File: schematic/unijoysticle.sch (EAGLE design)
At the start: 8 parts, among them IC1 4066N, IC2 4066N, IC3 4066N, J1 DB9, J2 DB9, J3 POWER_JACKSLT

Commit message: PCB fixes: reduced realstate
uses new DB9 connectors without the uneeded holes.
compabible with Commodore 128D and SX-64
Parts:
- J1, J2: device SparkFun-Connectors:DB9FEMALE -> riq-connectors:DB9FEMALE
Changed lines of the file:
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@@
 <part name="GND1" library="SparkFun-Aesthetics" deviceset="GND2" device=""/>
 <part name="GND2" library="SparkFun-Aesthetics" deviceset="GND2" device=""/>
-<part name="J1" library="SparkFun-Connectors" deviceset="DB9" device="FEMALE" value="DB9">
+<part name="J1" library="riq-connectors" deviceset="DB9" device="FEMALE" value="DB9">
 <attribute name="MF" value=""/>
 <attribute name="MPN" value="618009231121"/>
 <attribute name="OC_NEWARK" value="16T0655"/>
 </part>
-<part name="J2" library="SparkFun-Connectors" deviceset="DB9" device="FEMALE" value="DB9">
+<part name="J2" library="riq-connectors" deviceset="DB9" device="FEMALE" value="DB9">
 <attribute name="MF" value=""/>
 <attribute name="MPN" value="618009231121"/>

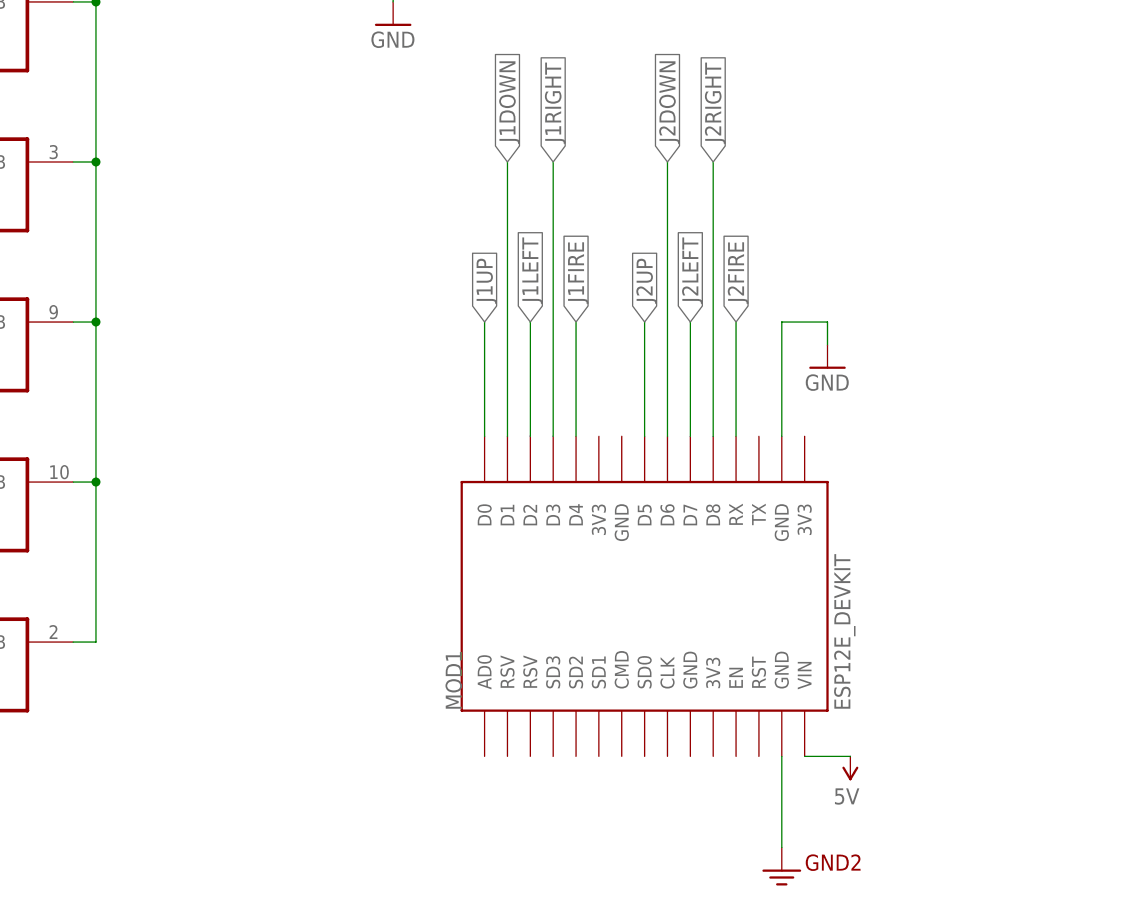
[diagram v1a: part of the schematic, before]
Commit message: using wemos d1 mini instead of NodeMCU
smaller realstate PCB making it under 5cm by 5cm.
cheaper to order from certain providers
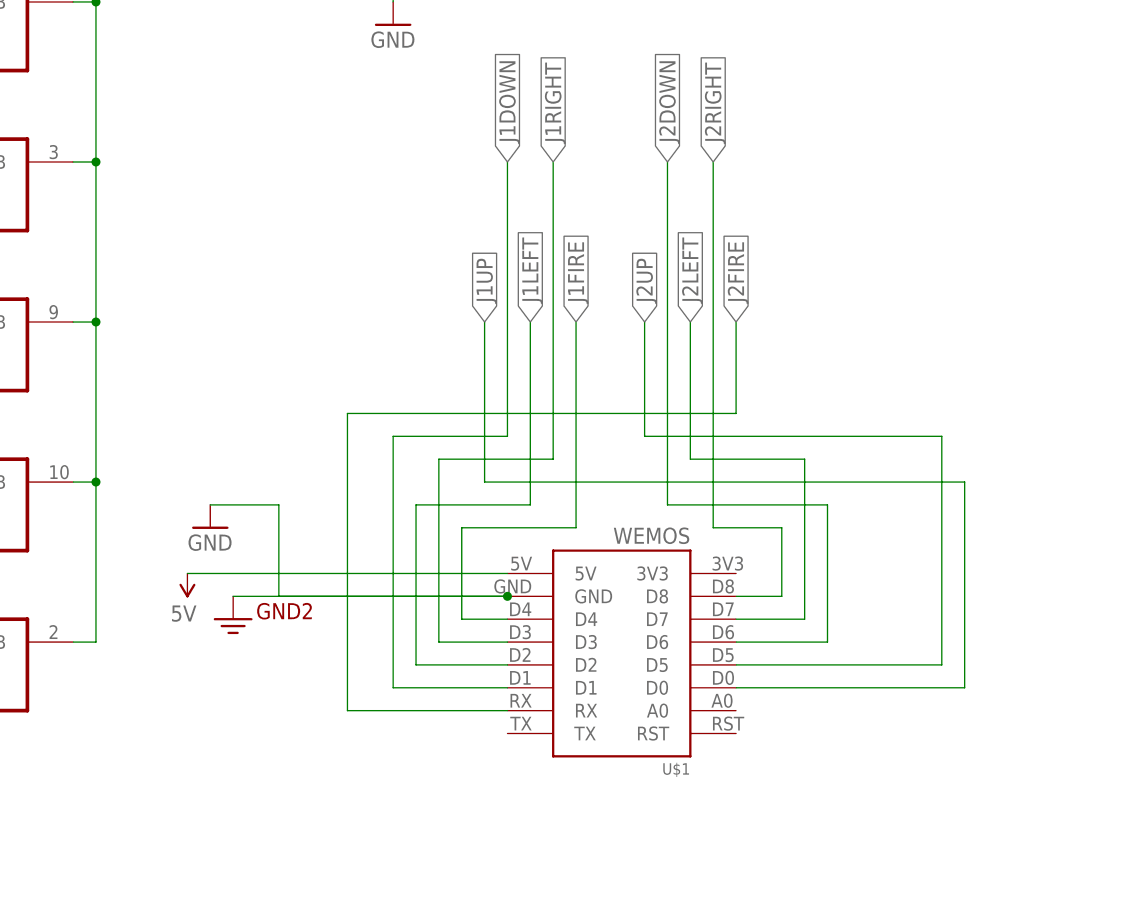
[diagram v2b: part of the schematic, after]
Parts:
- removed MOD1: ESP12E_DEVKIT, ESP12E_DEVKIT:ESP12E_DEVKIT
- added U$1: WEMOS, 1455413453956-wemos:WEMOS
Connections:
- net 3.3V: no longer MOD1.GND@1
- net 5V: now also U$1.5V; no longer MOD1.VIN
- net GND: now also U$1.GND; no longer MOD1.GND@3
- net J1DOWN: now also U$1.D1; no longer MOD1.D1
- net J1FIRE: now also U$1.D4; no longer MOD1.D4
- net J1LEFT: now also U$1.D2; no longer MOD1.D2
- net J1RIGHT: now also U$1.D3; no longer MOD1.D3
- net J1UP: now also U$1.D0; no longer MOD1.D0
- net J2DOWN: now also U$1.D6; no longer MOD1.D6
- net J2FIRE: now also U$1.RX; no longer MOD1.RX
- net J2LEFT: now also U$1.D7; no longer MOD1.D7
- net J2RIGHT: now also U$1.D8; no longer MOD1.D8
- net J2UP: now also U$1.D5; no longer MOD1.D5
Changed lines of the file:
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@@
 <attributes>
 <attribute name="CNAME" value="Retro Moe"/>
-<attribute name="CREVISION" value="0.2.2"/>
+<attribute name="CREVISION" value="0.3.2"/>
 <attribute name="DESIGNER" value="Ricardo Quesada"/>
 </attributes>
@@
 <attribute name="OC_NEWARK" value="16T0655"/>
 </part>
-<part name="MOD1" library="ESP12E_DEVKIT" deviceset="ESP12E_DEVKIT" device=""/>
 <part name="FRAME1" library="SparkFun-Aesthetics" deviceset="FRAME-A4L" device=""/>
 <part name="J3" library="SparkFun-Connectors" deviceset="POWER_JACK" device="SLT"/>
@@
 <part name="GND5" library="SparkFun-Aesthetics" deviceset="GND" device=""/>
 <part name="GND6" library="SparkFun-Aesthetics" deviceset="GND" device=""/>
+<part name="U$1" library="1455413453956-wemos" deviceset="WEMOS" device=""/>
 </parts>
 <sheets>
@@
 <instance part="IC1" gate="P" x="101.6" y="142.24"/>
 <instance part="IC3" gate="P" x="109.22" y="139.7"/>
-<instance part="GND3" gate="1" x="149.86" y="86.36"/>
+<instance part="GND3" gate="1" x="81.28" y="68.58"/>
 <instance part="GND4" gate="1" x="101.6" y="124.46"/>
 <instance part="IC2" gate="A" x="53.34" y="53.34">
@@
 </instance>
 <instance part="SUPPLY1" gate="G$1" x="175.26" y="144.78"/>
-<instance part="SUPPLY2" gate="G$1" x="152.4" y="43.18" rot="R180"/>
+<instance part="SUPPLY2" gate="G$1" x="78.74" y="63.5" rot="R180"/>
 <instance part="GND1" gate="G$1" x="177.8" y="137.16"/>
-<instance part="GND2" gate="G$1" x="144.78" y="30.48"/>
+<instance part="GND2" gate="G$1" x="83.82" y="58.42"/>
 <instance part="J1" gate="G$1" x="53.34" y="157.48">
 <attribute name="OC_NEWARK" x="53.34" y="157.48" size="1.778" layer="96" display="off"/>
@@
 <attribute name="MPN" x="233.68" y="152.4" size="1.778" layer="96" display="off"/>
 </instance>
-<instance part="MOD1" gate="G$1" x="129.54" y="60.96" rot="R90"/>
 <instance part="FRAME1" gate="G$1" x="0" y="0"/>
 <instance part="J3" gate="G$1" x="144.78" y="137.16"/>
@@
 <instance part="GND5" gate="1" x="256.54" y="147.32"/>
 <instance part="GND6" gate="1" x="76.2" y="152.4"/>
+<instance part="U$1" gate="G$1" x="134.62" y="66.04" rot="R180"/>
 </instances>
 <busses>
@@
 </segment>
 <segment>
-<pinref part="MOD1" gate="G$1" pin="D0"/>
-<wire x1="111.76" y1="78.74" x2="111.76" y2="91.44" width="0.1524" layer="91"/>
+<wire x1="111.76" y1="73.66" x2="111.76" y2="91.44" width="0.1524" layer="91"/>
 <label x="111.76" y="91.44" size="1.778" layer="95" rot="R90" xref="yes"/>
+<wire x1="111.76" y1="73.66" x2="165.1" y2="73.66" width="0.1524" layer="91"/>
+<wire x1="165.1" y1="73.66" x2="165.1" y2="50.8" width="0.1524" layer="91"/>
+<pinref part="U$1" gate="G$1" pin="D0"/>
+<wire x1="165.1" y1="50.8" x2="139.7" y2="50.8" width="0.1524" layer="91"/>
 </segment>
 </net>
@@
 </segment>
 <segment>
-<pinref part="MOD1" gate="G$1" pin="D1"/>
 <label x="114.3" y="109.22" size="1.778" layer="95" rot="R90" xref="yes"/>
 <wire x1="114.3" y1="78.74" x2="114.3" y2="109.22" width="0.1524" layer="91"/>
+<wire x1="114.3" y1="78.74" x2="101.6" y2="78.74" width="0.1524" layer="91"/>
+<wire x1="101.6" y1="78.74" x2="101.6" y2="50.8" width="0.1524" layer="91"/>
+<pinref part="U$1" gate="G$1" pin="D1"/>
+<wire x1="101.6" y1="50.8" x2="114.3" y2="50.8" width="0.1524" layer="91"/>
 </segment>
 </net>
@@
 </segment>
 <segment>
-<wire x1="116.84" y1="78.74" x2="116.84" y2="91.44" width="0.1524" layer="91"/>
-<pinref part="MOD1" gate="G$1" pin="D2"/>
+<wire x1="116.84" y1="71.12" x2="116.84" y2="91.44" width="0.1524" layer="91"/>
 <label x="116.84" y="91.44" size="1.778" layer="95" rot="R90" xref="yes"/>
+<wire x1="116.84" y1="71.12" x2="104.14" y2="71.12" width="0.1524" layer="91"/>
+<wire x1="104.14" y1="71.12" x2="104.14" y2="53.34" width="0.1524" layer="91"/>
+<pinref part="U$1" gate="G$1" pin="D2"/>
+<wire x1="104.14" y1="53.34" x2="114.3" y2="53.34" width="0.1524" layer="91"/>
 </segment>
 </net>
@@
 </segment>
 <segment>
-<pinref part="MOD1" gate="G$1" pin="D3"/>
 <label x="119.38" y="109.22" size="1.778" layer="95" rot="R90" xref="yes"/>
-<wire x1="119.38" y1="109.22" x2="119.38" y2="78.74" width="0.1524" layer="91"/>
+<wire x1="119.38" y1="109.22" x2="119.38" y2="76.2" width="0.1524" layer="91"/>
+<wire x1="119.38" y1="76.2" x2="106.68" y2="76.2" width="0.1524" layer="91"/>
+<wire x1="106.68" y1="76.2" x2="106.68" y2="55.88" width="0.1524" layer="91"/>
+<pinref part="U$1" gate="G$1" pin="D3"/>
+<wire x1="106.68" y1="55.88" x2="114.3" y2="55.88" width="0.1524" layer="91"/>
 </segment>
 </net>
@@
 </segment>
 <segment>
-<wire x1="144.78" y1="78.74" x2="144.78" y2="91.44" width="0.1524" layer="91"/>
-<wire x1="144.78" y1="91.44" x2="149.86" y2="91.44" width="0.1524" layer="91"/>
 <pinref part="GND3" gate="1" pin="GND"/>
-<wire x1="149.86" y1="91.44" x2="149.86" y2="88.9" width="0.1524" layer="91"/>
-<pinref part="MOD1" gate="G$1" pin="GND@3"/>
+<pinref part="GND2" gate="G$1" pin="3.3V"/>
+<wire x1="83.82" y1="60.96" x2="114.3" y2="60.96" width="0.1524" layer="91"/>
+<pinref part="U$1" gate="G$1" pin="GND"/>
+<wire x1="81.28" y1="71.12" x2="88.9" y2="71.12" width="0.1524" layer="91"/>
+<wire x1="88.9" y1="71.12" x2="88.9" y2="60.96" width="0.1524" layer="91"/>
+<wire x1="88.9" y1="60.96" x2="114.3" y2="60.96" width="0.1524" layer="91"/>
+<junction x="114.3" y="60.96"/>
 </segment>
 <segment>
@@
 <segment>
 <pinref part="SUPPLY2" gate="G$1" pin="5V"/>
-<wire x1="152.4" y1="43.18" x2="147.32" y2="43.18" width="0.1524" layer="91"/>
-<pinref part="MOD1" gate="G$1" pin="VIN"/>
+<wire x1="78.74" y1="63.5" x2="114.3" y2="63.5" width="0.1524" layer="91"/>
+<pinref part="U$1" gate="G$1" pin="5V"/>
 </segment>
 </net>
@@
 <junction x="147.32" y="139.7"/>
 </segment>
-<segment>
-<pinref part="GND2" gate="G$1" pin="3.3V"/>
-<wire x1="144.78" y1="33.02" x2="144.78" y2="43.18" width="0.1524" layer="91"/>
-<pinref part="MOD1" gate="G$1" pin="GND@1"/>
-</segment>
 </net>
 <net name="J1FIRE" class="0">
@@
 </segment>
 <segment>
-<wire x1="121.92" y1="91.44" x2="121.92" y2="78.74" width="0.1524" layer="91"/>
-<pinref part="MOD1" gate="G$1" pin="D4"/>
+<wire x1="121.92" y1="91.44" x2="121.92" y2="68.58" width="0.1524" layer="91"/>
 <label x="121.92" y="91.44" size="1.778" layer="95" rot="R90" xref="yes"/>
+<wire x1="121.92" y1="68.58" x2="109.22" y2="68.58" width="0.1524" layer="91"/>
+<wire x1="109.22" y1="68.58" x2="109.22" y2="58.42" width="0.1524" layer="91"/>
+<pinref part="U$1" gate="G$1" pin="D4"/>
+<wire x1="109.22" y1="58.42" x2="114.3" y2="58.42" width="0.1524" layer="91"/>
 </segment>
 </net>
 <net name="J2UP" class="0">
 <segment>
-<pinref part="MOD1" gate="G$1" pin="D5"/>
 <wire x1="129.54" y1="78.74" x2="129.54" y2="91.44" width="0.1524" layer="91"/>
 <label x="129.54" y="91.44" size="1.778" layer="95" rot="R90" xref="yes"/>
+<pinref part="U$1" gate="G$1" pin="D5"/>
+<wire x1="139.7" y1="53.34" x2="162.56" y2="53.34" width="0.1524" layer="91"/>
+<wire x1="162.56" y1="53.34" x2="162.56" y2="78.74" width="0.1524" layer="91"/>
+<wire x1="162.56" y1="78.74" x2="129.54" y2="78.74" width="0.1524" layer="91"/>
 </segment>
 <segment>
@@
 <net name="J2DOWN" class="0">
 <segment>
-<pinref part="MOD1" gate="G$1" pin="D6"/>
 <label x="132.08" y="109.22" size="1.778" layer="95" rot="R90" xref="yes"/>
-<wire x1="132.08" y1="109.22" x2="132.08" y2="78.74" width="0.1524" layer="91"/>
+<wire x1="132.08" y1="109.22" x2="132.08" y2="71.12" width="0.1524" layer="91"/>
+<wire x1="132.08" y1="71.12" x2="149.86" y2="71.12" width="0.1524" layer="91"/>
+<wire x1="149.86" y1="71.12" x2="149.86" y2="55.88" width="0.1524" layer="91"/>
+<pinref part="U$1" gate="G$1" pin="D6"/>
+<wire x1="149.86" y1="55.88" x2="139.7" y2="55.88" width="0.1524" layer="91"/>
 </segment>
 <segment>
@@
 <net name="J2LEFT" class="0">
 <segment>
-<pinref part="MOD1" gate="G$1" pin="D7"/>
-<wire x1="134.62" y1="78.74" x2="134.62" y2="91.44" width="0.1524" layer="91"/>
+<wire x1="134.62" y1="76.2" x2="134.62" y2="91.44" width="0.1524" layer="91"/>
 <label x="134.62" y="91.44" size="1.778" layer="95" rot="R90" xref="yes"/>
+<wire x1="134.62" y1="76.2" x2="147.32" y2="76.2" width="0.1524" layer="91"/>
+<wire x1="147.32" y1="76.2" x2="147.32" y2="58.42" width="0.1524" layer="91"/>
+<pinref part="U$1" gate="G$1" pin="D7"/>
+<wire x1="147.32" y1="58.42" x2="139.7" y2="58.42" width="0.1524" layer="91"/>
 </segment>
 <segment>
@@
 <net name="J2RIGHT" class="0">
 <segment>
-<pinref part="MOD1" gate="G$1" pin="D8"/>
 <label x="137.16" y="109.22" size="1.778" layer="95" rot="R90" xref="yes"/>
-<wire x1="137.16" y1="109.22" x2="137.16" y2="78.74" width="0.1524" layer="91"/>
+<pinref part="U$1" gate="G$1" pin="D8"/>
+<wire x1="137.16" y1="68.58" x2="144.78" y2="68.58" width="0.1524" layer="91"/>
+<wire x1="144.78" y1="68.58" x2="144.78" y2="60.96" width="0.1524" layer="91"/>
+<wire x1="144.78" y1="60.96" x2="139.7" y2="60.96" width="0.1524" layer="91"/>
+<wire x1="137.16" y1="109.22" x2="137.16" y2="68.58" width="0.1524" layer="91"/>
 </segment>
 <segment>
@@
 <net name="J2FIRE" class="0">
 <segment>
-<pinref part="MOD1" gate="G$1" pin="RX"/>
-<wire x1="139.7" y1="78.74" x2="139.7" y2="91.44" width="0.1524" layer="91"/>
+<wire x1="139.7" y1="81.28" x2="139.7" y2="91.44" width="0.1524" layer="91"/>
 <label x="139.7" y="91.44" size="1.778" layer="95" rot="R90" xref="yes"/>
+<wire x1="139.7" y1="81.28" x2="96.52" y2="81.28" width="0.1524" layer="91"/>
+<wire x1="96.52" y1="81.28" x2="96.52" y2="48.26" width="0.1524" layer="91"/>
+<pinref part="U$1" gate="G$1" pin="RX"/>
+<wire x1="96.52" y1="48.26" x2="114.3" y2="48.26" width="0.1524" layer="91"/>
 </segment>
 <segment>
@@
 </schematic>
 </drawing>
+<compatibility>
+<note version="6.3" minversion="6.2.2" severity="warning">
+Since Version 6.2.2 text objects can contain more than one line,
+which will not be processed correctly with this version.
+</note>
+</compatibility>
 </eagle>
